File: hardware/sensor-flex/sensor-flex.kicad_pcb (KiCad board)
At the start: 4 copper layers, 27.3 x 19.1 mm, 34 parts, among them IC1 VCNL4040M3OE, IC2 VCNL4040M3OE, J1 Conn_01x05, U1 PCA9546APWR

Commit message: Interrupts and new flex design
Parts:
- removed C1: 2.2µF, Capacitor_SMD:C_0603_1608Metric
- removed C2: 0.1µF, Capacitor_SMD:C_0603_1608Metric
- removed D1: LED, LED_SMD:LED_0603_1608Metric
- removed D2, D3: BAT54S, Package_TO_SOT_SMD:SOT-23
- removed J1: Conn_01x05, Connector_JST:JST_SH_SM05B-SRSS-TB_1x05-1MP_P1.00mm_Horizontal
- removed JP3, JP4: SolderJumper_2_Open, Jumper:SolderJumper-2_P1.3mm_Open_RoundedPad1.0x1.5mm
- removed R1, R2, R6, R7, R8, R9: 4.7kΩ, Resistor_SMD:R_0603_1608Metric
- removed R12, R13, R14, R3: 10kΩ, Resistor_SMD:R_0603_1608Metric
- removed R4: 1kΩ, Resistor_SMD:R_0603_1608Metric
- removed R5: 8.2kΩ, Resistor_SMD:R_0603_1608Metric
- removed TP1, TP2, TP3, TP4, TP5: TestPoint_Small, TestPoint:TestPoint_Pad_D1.5mm
- removed U1: PCA9546APWR, motion-play-footprints:SOP65P640X120-16N
- added FPC1: FPC_Tail_10P, motion-play-footprints:FPC_Tail_10P_1.0mm_TopContact, F.Cu at (117.7, 93.2)
- moved C6 48.9 mm to (170.8, 95.3)
- moved C4 48.4 mm to (170.8, 91.7), turned to 90 degrees
- moved R10 48.4 mm to (172.4, 92.7)
- moved IC2 48.0 mm to (167.5, 92.7)
- moved C8 44.6 mm to (160.0, 91.7), turned to 90 degrees
- moved C7 44.1 mm to (160.0, 95.2)
- moved IC1 43.4 mm to (156.7, 92.7)
- moved R11 43.3 mm to (161.6, 92.7)
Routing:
- net Net-(FPC1-INT2): track 3.05 -> 49.3 mm
- net +3.3V: track 32.1 -> 74.7 mm, vias 18 -> 0
- net Net-(FPC1-SCL2): track 7.99 -> 50.3 mm
- net Net-(FPC1-SDA2): track 9.24 -> 49.8 mm
- net Net-(FPC1-INT1): track 3.22 -> 37.7 mm
- net Net-(FPC1-SCL1): track 7.46 -> 37.6 mm
- net Net-(D2-A): track 29.0 -> 0.00 mm
- net Net-(FPC1-SDA1): track 11.1 -> 37.7 mm
- net Net-(J1-Pin_3): track 19.2 -> 0.00 mm
- net Net-(J1-Pin_4): track 18.0 -> 0.00 mm
- net GND: track 21.1 -> 11.9 mm, vias 14 -> 7
- net Net-(JP3-A): track 6.37 -> 0.00 mm
- net Net-(U1-~{RESET}): track 6.19 -> 0.00 mm
- net Net-(D1-A): track 5.57 -> 0.00 mm
- net Net-(JP4-A): track 4.70 -> 0.00 mm
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- added copper zone on B.Cu, net GND
- removed copper zone on In2.Cu, net +3.3V
- removed copper zone on In1.Cu, net GND
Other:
- board size 27.3 x 19.1 mm -> 57.1 x 10.2 mm
- copper layers 4 -> 2
- board text added: "3.3V"
- board text added: "COMPONENT STIFFENER 1 (IC1 area) Material: FR4 Thickness: 0.5mm Side: Bottom COMPONENT STIFFENER 2 (IC2 area) Material: FR4 Thickness: 0.5mm Side: Bottom"
- board text added: "FPC TAIL STIFFENER: PI (Polyimide), 0.2mm thick, BOTTOM side Target total thickness: 0.3mm"
- board text added: "IC1"
- board text added: "IC2"
- board text added: "IN1"
- board text added: "IN2"
- board text added: "SC1"
- board text added: "SC2"
- board text added: "SD1"
- board text added: "SD2"
- board text removed: "3.3v"
- board text removed: "INT"
- board text removed: "SC"
- board text removed: "SD"

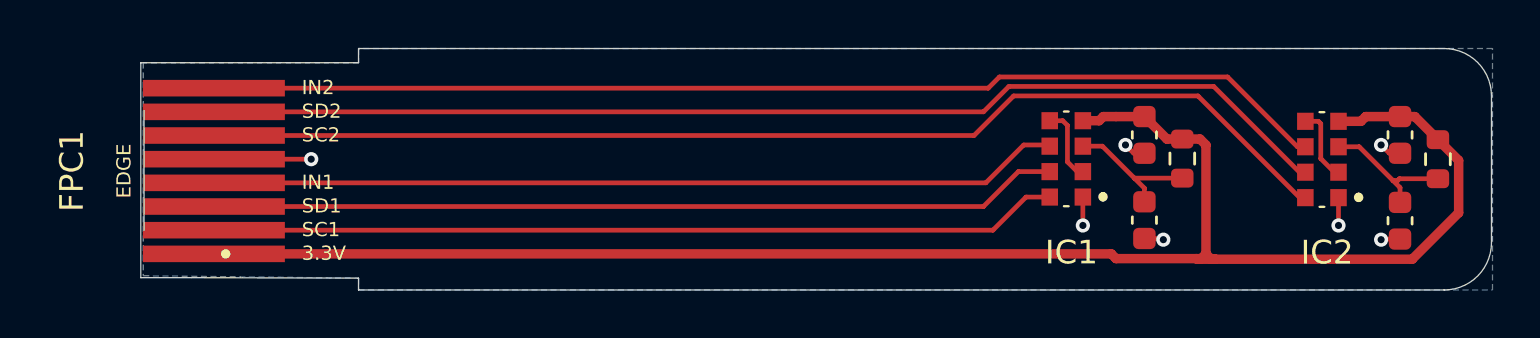
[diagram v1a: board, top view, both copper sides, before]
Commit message: Added documentation for calibration feature, and latest PCB design changes
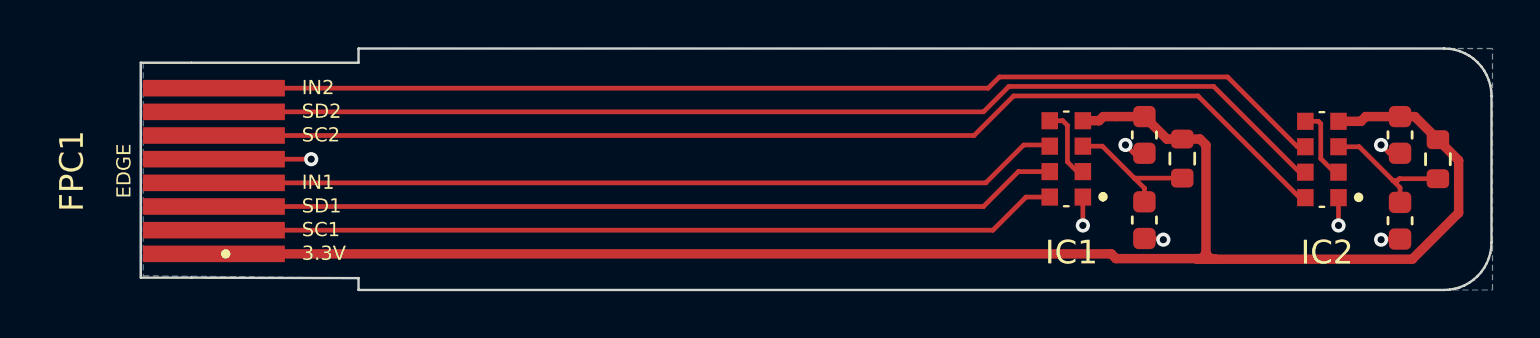
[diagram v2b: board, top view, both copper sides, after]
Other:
- outline, holes or cut-outs redrawn
- board text added: "COMPONENT STIFFENER 1 (IC1 area) Material: FR4 Thickness: 0.6mm Side: Bottom COMPONENT STIFFENER 2 (IC2 area) Material: FR4 Thickness: 0.6mm Side: Bottom"
- board text added: "FPC TAIL STIFFENER: PI (Polyimide) BOTTOM side Target total thickness: 0.3mm"
- board text removed: "COMPONENT STIFFENER 1 (IC1 area) Material: FR4 Thickness: 0.5mm Side: Bottom COMPONENT STIFFENER 2 (IC2 area) Material: FR4 Thickness: 0.5mm Side: Bottom"
- board text removed: "FPC TAIL STIFFENER: PI (Polyimide), 0.2mm thick, BOTTOM side Target total thickness: 0.3mm"
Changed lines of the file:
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@@
 		)
 	)
-	(gr_line
-		(start 119.7375 88.6)
-		(end 126.8 88.6)
+	(gr_poly
+		(pts
+			(xy 126.8 88.6) (xy 119.7375 88.6) (xy 117.6 88.6) (xy 117.6 97.680502) (xy 119.731983 97.680502)
+			(xy 126.8 97.7) (xy 126.8 98.2)
+			(arc
+				(start 172.6625 98.2)
+				(mid 174.076714 97.614214)
+				(end 174.6625 96.2)
+			)
+			(arc
+				(start 174.6625 90)
+				(mid 174.076714 88.585786)
+				(end 172.6625 88)
+			)
+			(xy 126.8 88)
+		)
 		(stroke
-			(width 0.05)
-			(type default)
+			(width 0.1)
+			(type solid)
 		)
-		(layer "Edge.Cuts")
-	)
-	(gr_arc
-		(start 172.6625 88)
-		(mid 174.076714 88.585786)
-		(end 174.6625 90)
-		(stroke
-			(width 0.05)
-			(type default)
-		)
-		(layer "Edge.Cuts")
-	)
-	(gr_line
-		(start 117.6 97.680502)
-		(end 119.731983 97.680502)
-		(stroke
-			(width 0.05)
-			(type default)
-		)
-		(layer "Edge.Cuts")
-	)
-	(gr_line
-		(start 126.8 97.7)
-		(end 119.731983 97.680502)
-		(stroke
-			(width 0.05)
-			(type default)
-		)
-		(layer "Edge.Cuts")
-	)
-	(gr_line
-		(start 126.8 88)
-		(end 172.6625 88)
-		(stroke
-			(width 0.05)
-			(type default)
-		)
-		(layer "Edge.Cuts")
-	)
-	(gr_line
-		(start 119.7375 88.6)
-		(end 117.6 88.6)
-		(stroke
-			(width 0.05)
-			(type default)
-		)
-		(layer "Edge.Cuts")
-	)
-	(gr_line
-		(start 117.6 88.6)
-		(end 117.6 97.680502)
-		(stroke
-			(width 0.05)
-			(type default)
-		)
-		(layer "Edge.Cuts")
-	)
-	(gr_line
-		(start 117.7375 95.68051)
-		(end 117.7375 90.6)
-		(stroke
-			(width 0.05)
-			(type default)
-		)
-		(layer "Edge.Cuts")
-	)
-	(gr_arc
-		(start 174.6625 96.2)
-		(mid 174.076714 97.614214)
-		(end 172.6625 98.2)
-		(stroke
-			(width 0.05)
-			(type default)
-		)
-		(layer "Edge.Cuts")
-	)
-	(gr_line
-		(start 172.6625 98.2)
-		(end 126.8 98.2)
-		(stroke
-			(width 0.05)
-			(type default)
-		)
-		(layer "Edge.Cuts")
-	)
-	(gr_line
-		(start 126.8 98.2)
-		(end 126.8 97.7)
-		(stroke
-			(width 0.05)
-			(type default)
-		)
-		(layer "Edge.Cuts")
-	)
-	(gr_line
-		(start 174.6625 90)
-		(end 174.6625 96.2)
-		(stroke
-			(width 0.05)
-			(type default)
-		)
-		(layer "Edge.Cuts")
-	)
-	(gr_line
-		(start 126.8 88.6)
-		(end 126.8 88)
-		(stroke
-			(width 0.05)
-			(type default)
-		)
+		(fill no)
 		(layer "Edge.Cuts")
 	)
@@
 		)
 	)
-	(gr_text "COMPONENT STIFFENER 1 (IC1 area)\nMaterial: FR4\nThickness: 0.5mm\nSide: Bottom\n\nCOMPONENT STIFFENER 2 (IC2 area)\nMaterial: FR4\nThickness: 0.5mm\nSide: Bottom"
+	(gr_text "COMPONENT STIFFENER 1 (IC1 area)\nMaterial: FR4\nThickness: 0.6mm\nSide: Bottom\n\nCOMPONENT STIFFENER 2 (IC2 area)\nMaterial: FR4\nThickness: 0.6mm\nSide: Bottom"
 		(at 157.8 113.875 0)
 		(layer "Cmts.User")
@@
 		)
 	)
-	(gr_text "FPC TAIL STIFFENER: \nPI (Polyimide), 0.2mm thick, \nBOTTOM side\nTarget total thickness: 0.3mm"
+	(gr_text "FPC TAIL STIFFENER: \nPI (Polyimide)\nBOTTOM side\nTarget total thickness: 0.3mm"
 		(at 116.6 84.8 0)
 		(layer "Cmts.User")

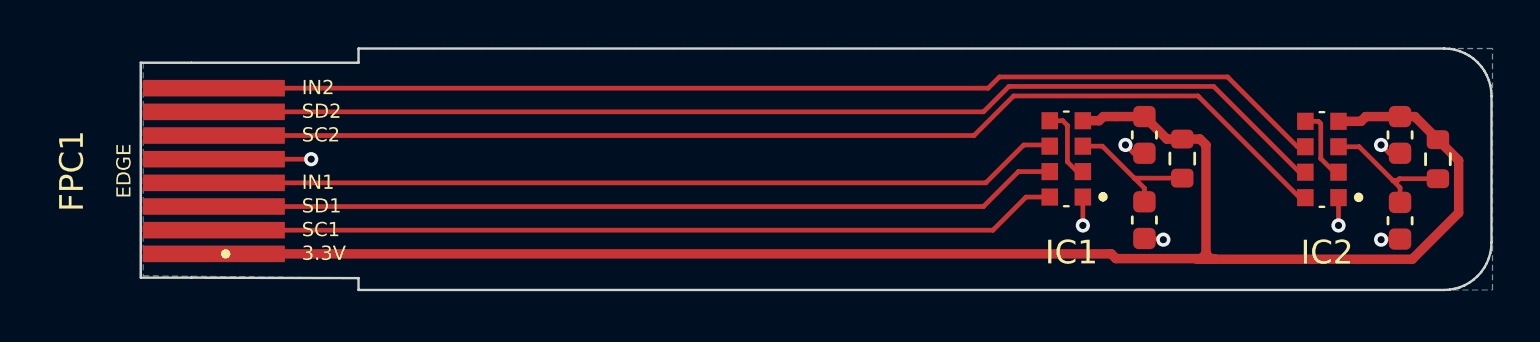
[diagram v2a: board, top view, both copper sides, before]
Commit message: Hardware revision: remove interrupts, update connectors, add DIP switch
Remove INT lines from all three PCBs (main, rigid, flex). Replace 5-pin
JST-SH connectors with 4-pin SM04B-SRSS-TB on main and rigid boards.
Replace solder jumpers with EP-02KS DIP switch for I2C address config
on rigid board. Update FPC connector pinout to remove INT signals and
add GND fills. Update stiffener specs (PI 0.25mm tail, SS 0.2mm IC
areas). Regenerate production files (BOM, CPL) for both sensor boards.
Update hardware CONTEXT.md with corrected addresses (0x74-0x76),
component tables, and pinouts.

Made-with: Cursor
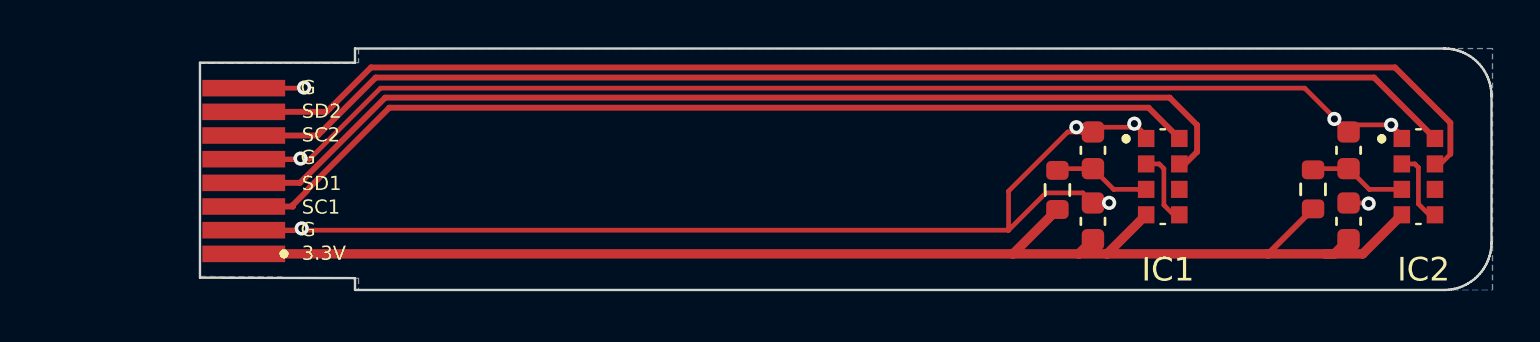
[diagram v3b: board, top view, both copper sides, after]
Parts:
- moved R11 5.44 mm to (156.3, 94.0), turned to 90 degrees
- moved R10 5.43 mm to (167.1, 94.0)
- moved C4 4.25 mm to (168.6, 95.3), turned to -90 degrees
- moved C8 4.25 mm to (157.8, 95.3), turned to -90 degrees
- moved IC1 4.14 mm to (160.8, 93.4), turned to 180 degrees
- moved IC2 4.14 mm to (171.6, 93.4), turned to 180 degrees
- moved C6 3.69 mm to (168.6, 92.3), turned to 90 degrees
- moved C7 3.67 mm to (157.8, 92.3), turned to 90 degrees
- moved FPC1 2.46 mm to (120.2, 93.2)
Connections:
- net Net-(FPC1-SCL2) renamed /SCL2
- net Net-(FPC1-SDA2) renamed /SDA2
- net Net-(IC1-K(LED)) renamed /LED_K1
- net Net-(IC1-VDD) renamed /VDD_S1
- net Net-(IC2-K(LED)) renamed /LED_K2
- C6 pad 1: Net-(IC2-VDD) -> /VDD_S2
- FPC1 pad 2: Net-(FPC1-SCL1) -> GND
- FPC1 pad 3: Net-(FPC1-SDA1) -> /SCL1
- FPC1 pad 4: Net-(FPC1-INT1) -> /SDA1
- FPC1 pad 8: Net-(FPC1-INT2) -> GND
- IC1 pad 6: Net-(FPC1-INT1) -> unconnected-(IC1-INT-Pad6)
- IC1 pad 7: Net-(FPC1-SDA1) -> /SDA1
- IC1 pad 8: Net-(FPC1-SCL1) -> /SCL1
- IC2 pad 3: Net-(IC2-VDD) -> /VDD_S2
- IC2 pad 6: Net-(FPC1-INT2) -> unconnected-(IC2-INT-Pad6)
- R10 pad 1: +3.3V -> /VDD_S2
- R10 pad 2: Net-(IC2-VDD) -> +3.3V
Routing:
- net GND: track 11.9 -> 109.1 mm, vias 7 -> 9
- net Net-(FPC1-INT2): track 49.3 -> 0.00 mm
- net /SDA1: track 0.00 -> 44.3 mm
- net /SCL1: track 0.00 -> 41.8 mm
- net Net-(FPC1-INT1): track 37.7 -> 0.00 mm
- net Net-(FPC1-SDA1): track 37.7 -> 0.00 mm
- net Net-(FPC1-SCL1): track 37.6 -> 0.00 mm
- net +3.3V: track 74.7 -> 59.4 mm
- net Net-(IC2-VDD): track 5.87 -> 0.00 mm
- net /SDA2: track 49.8 -> 54.9 mm
- net /VDD_S2: track 0.00 -> 4.13 mm
- net /SCL2: track 50.3 -> 52.4 mm
- net /VDD_S1: track 5.94 -> 4.14 mm
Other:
- board size 57.1 x 10.2 mm -> 54.6 x 10.2 mm
- board text added: "COMPONENT STIFFENER (IC1) Material: Stainless Steel Thickness: 0.2mm Side: Bottom COMPONENT STIFFENER (IC1) Material: Stainless Steel Thickness: 0.2mm Side: Bottom"
- board text added: "G"
- board text added: "TAIL STIFFENER (FPC1) Material: PI (Polyimide) Thickness: 0.25mm Side: Bottom"
- board text removed: "COMPONENT STIFFENER 1 (IC1 area) Material: FR4 Thickness: 0.6mm Side: Bottom COMPONENT STIFFENER 2 (IC2 area) Material: FR4 Thickness: 0.6mm Side: Bottom"
- board text removed: "FPC TAIL STIFFENER: PI (Polyimide) BOTTOM side Target total thickness: 0.3mm"
- board text removed: "IN1"
- board text removed: "IN2"
